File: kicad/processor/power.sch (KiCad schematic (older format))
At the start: 32 parts, among them J2 V_QI, J3 GND, J4 Battery, Q1 DMG3415U, Q2 DMG3415U, Q3 DMG3414U, Q4 DMG3415U, Q5 DMG3415U, SW1 SW, U4 MCP73832, U5 NCP694-3.3

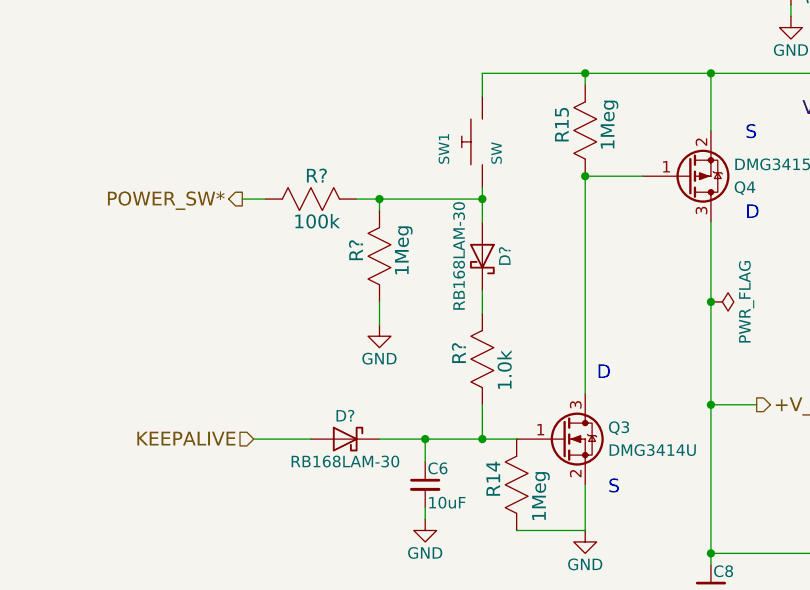
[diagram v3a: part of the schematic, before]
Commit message: start processor layout - footprint fixes
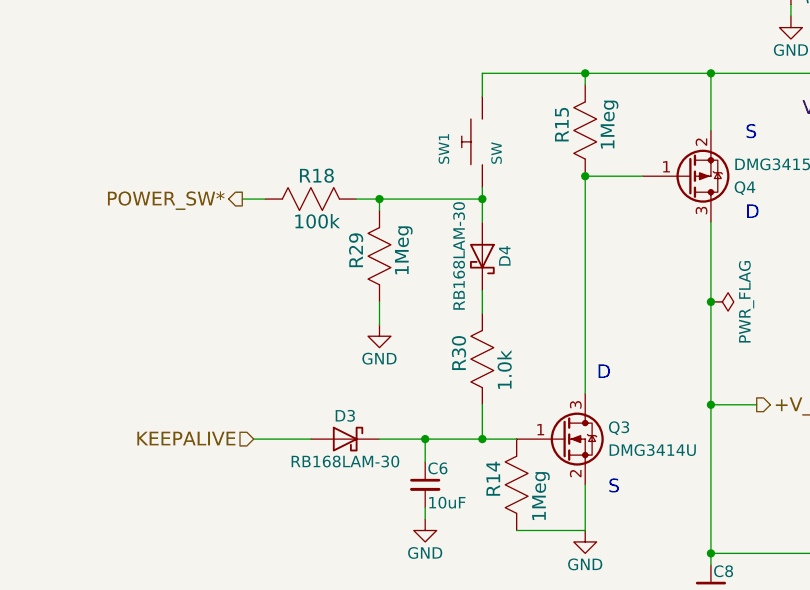
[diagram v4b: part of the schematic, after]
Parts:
- gave numbers to parts that had none: 5
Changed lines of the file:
@@
 Connection ~ 4450 1850
 $Comp
-L Schottky D?
+L Schottky D4
 U 1 1 5A0BC7B3
 P 5700 4450
-F 0 "D?" H 5700 4550 50  0000 C CNN
+F 0 "D4" H 5700 4550 50  0000 C CNN
 F 1 "RB168LAM-30" H 5700 4350 50  0000 C CNN
 F 2 "paddle:D_SOD-128" H 5700 4275 50  0001 C CNN
@@
 $EndComp
 $Comp
-L Schottky D?
+L Schottky D3
 U 1 1 5A0BC847
 P 5100 5250
-F 0 "D?" H 5100 5350 50  0000 C CNN
+F 0 "D3" H 5100 5350 50  0000 C CNN
 F 1 "RB168LAM-30" H 5100 5150 50  0000 C CNN
 F 2 "paddle:D_SOD-128" H 5100 5075 50  0001 C CNN
@@
 Connection ~ 6150 3650
 $Comp
-L R_US R?
+L R_US R30
 U 1 1 5A0BD110
 P 5700 4900
-F 0 "R?" H 5725 5000 60  0000 C CNN
+F 0 "R30" H 5725 5000 60  0000 C CNN
 F 1 "1.0k" H 5650 4800 60  0000 C CNN
 F 2 "paddle:R_0603" H 5700 4550 60  0001 C CNN
@@
 	5700 5100 5700 5250
 $Comp
-L R_US R?
+L R_US R29
 U 1 1 5A0BD777
 P 5250 4450
-F 0 "R?" H 5275 4550 60  0000 C CNN
+F 0 "R29" H 5275 4550 60  0000 C CNN
 F 1 "1Meg" H 5275 4350 60  0000 C CNN
 F 2 "paddle:R_0603" H 5250 4100 60  0001 C CNN
@@
 	5700 3650 7650 3650
 $Comp
-L R_US R?
+L R_US R18
 U 1 1 5A0BE1FB
 P 4950 4200
-F 0 "R?" H 4975 4300 60  0000 C CNN
+F 0 "R18" H 4975 4300 60  0000 C CNN
 F 1 "100k" H 4975 4100 60  0000 C CNN
 F 2 "paddle:R_0603" H 4950 3850 60  0001 C CNN

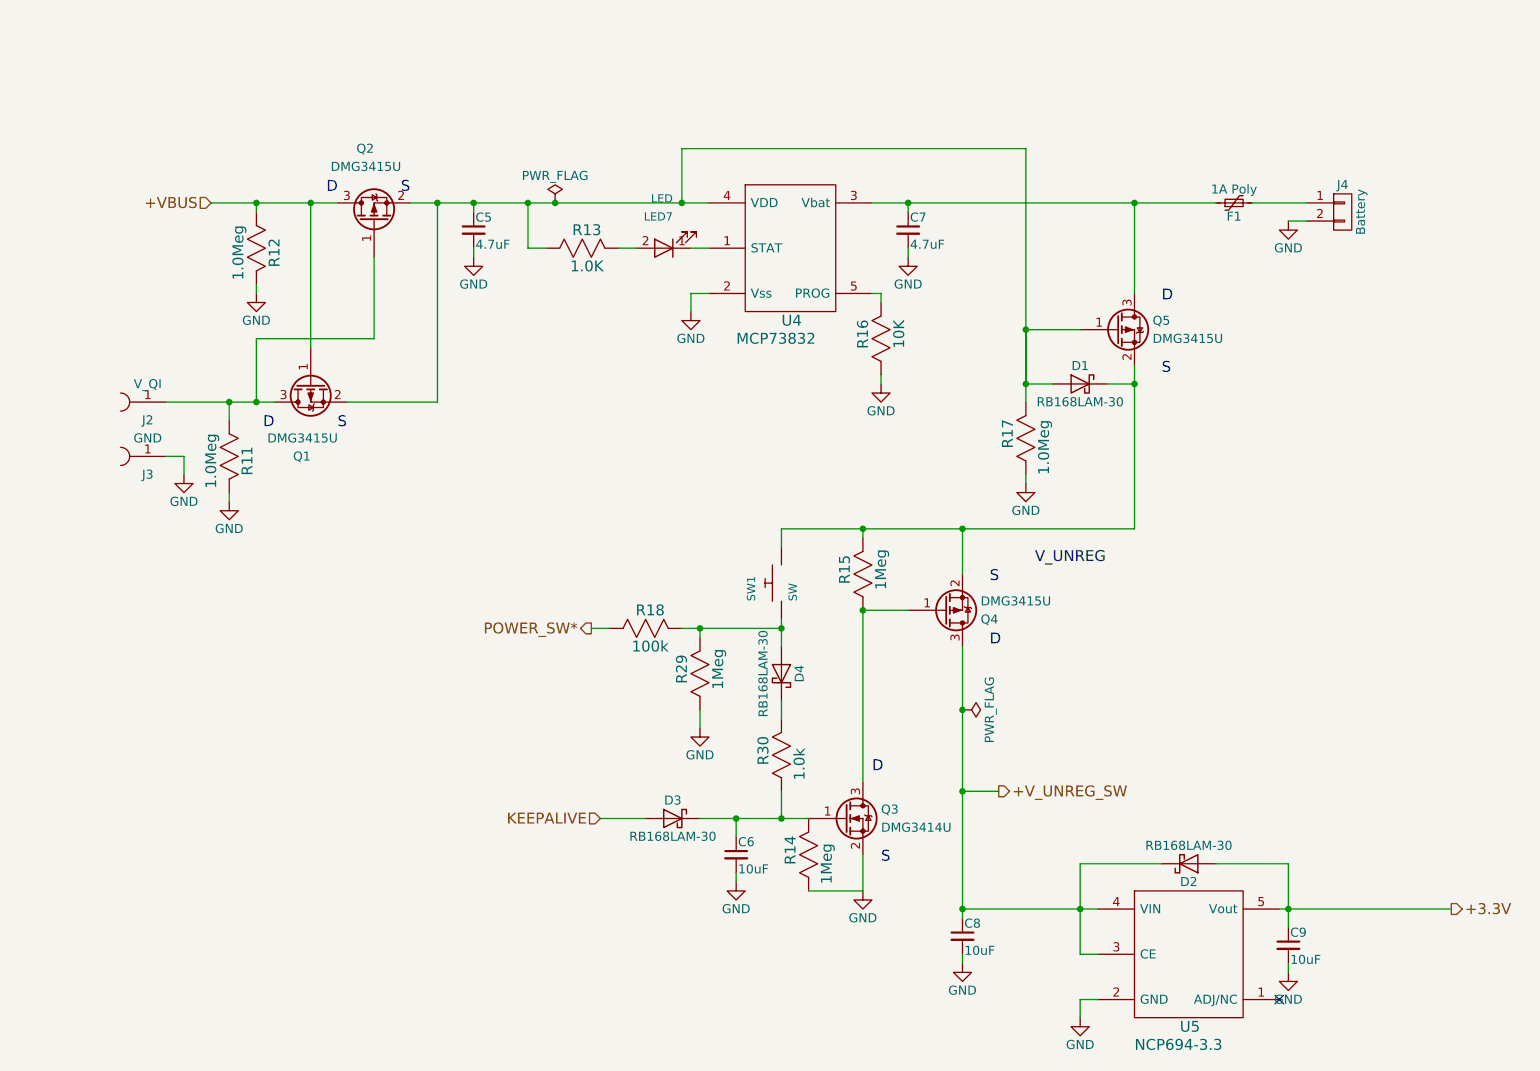
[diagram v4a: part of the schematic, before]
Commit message: First cut layout power supply, fix netclasses, footprint for connector
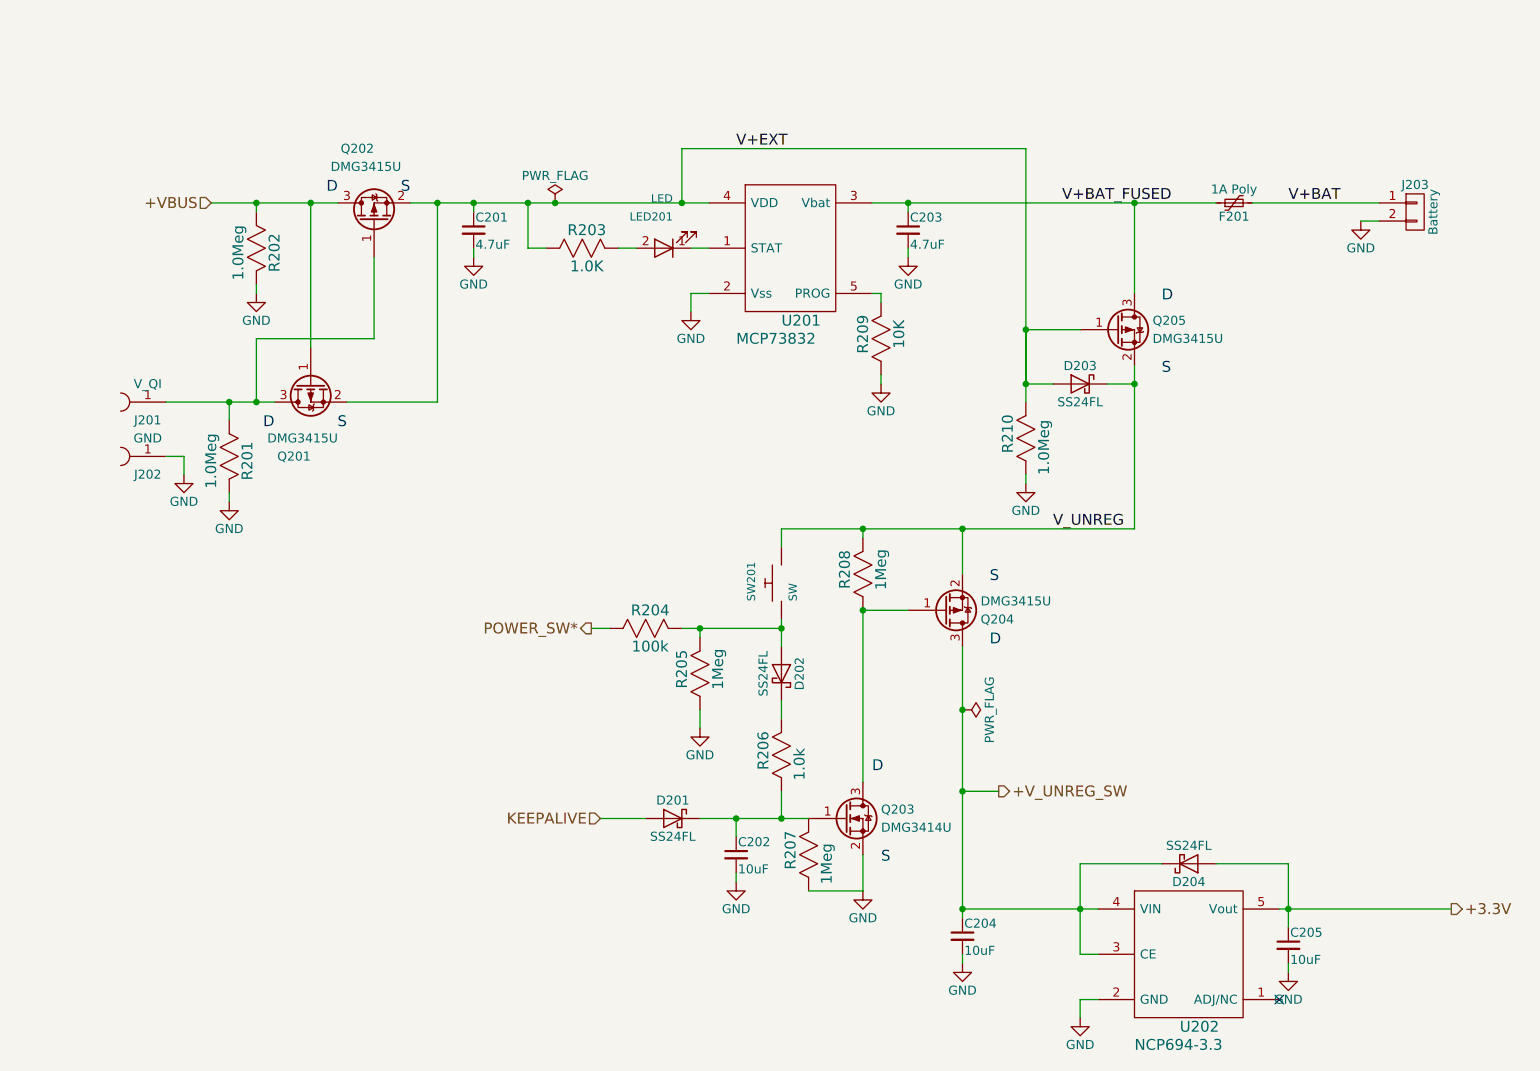
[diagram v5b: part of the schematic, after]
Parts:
- removed D1, D3, D4: RB168LAM-30, paddle:D_SOD-128, symbol Schottky
- added D201, D202, D203: SS24FL, paddle:D_SOD-123, symbol Schottky
- D204: renamed from D2; value RB168LAM-30 -> SS24FL; footprint paddle:D_SOD-128 -> paddle:D_SOD-123
- renumbered C5 to C201, C6 to C202, C7 to C203, C8 to C204, C9 to C205, F1 to F201, J2 to J201, J3 to J202, J4 to J203, LED7 to LED201, Q1 to Q201, Q2 to Q202, Q3 to Q203, Q4 to Q204, Q5 to Q205, R11 to R201, R12 to R202, R13 to R203, R18 to R204, R29 to R205, R30 to R206, R14 to R207, R15 to R208, R16 to R209, R17 to R210, SW1 to SW201, U4 to U201, U5 to U202
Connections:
- net KEEPALIVE: now also D201.1
- net V_UNREG: now also Q204.2 (S), Q205.2 (S), R208.2, SW201.2, D203.2
- net V+BAT: now reaches F201.2, J203.1 (P1)
- net V+BAT_FUSED: now reaches C203.1, F201.1, Q205.3 (D), U201.3 (Vbat)
- net at C202.1, Q203.1 (G), R206.1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: now also D201.2
- net V+EXT: now reaches C201.1, Q201.2 (S), Q202.2 (S), Q205.1 (G), R203.1, R210.2, U201.4 (VDD)
- net V+EXT: now also D203.1
- net at R204.2, R205.2, SW201.1: now also D202.1
- net at R206.2: now also D202.2
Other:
- moved on the sheet: J203
